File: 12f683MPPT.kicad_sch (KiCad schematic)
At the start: 47 parts, among them J1 Conn_01x01_Male, J2 Conn_01x01_Male, J3 Conn_01x01_Male, J4 Conn_01x01_Male, Q1 BUK9511-55A127, Q2 BUK9511-55A127, Q3 2N2222A, Q4 2N2222A, Q5 2N2907A, SW1 SW_Push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

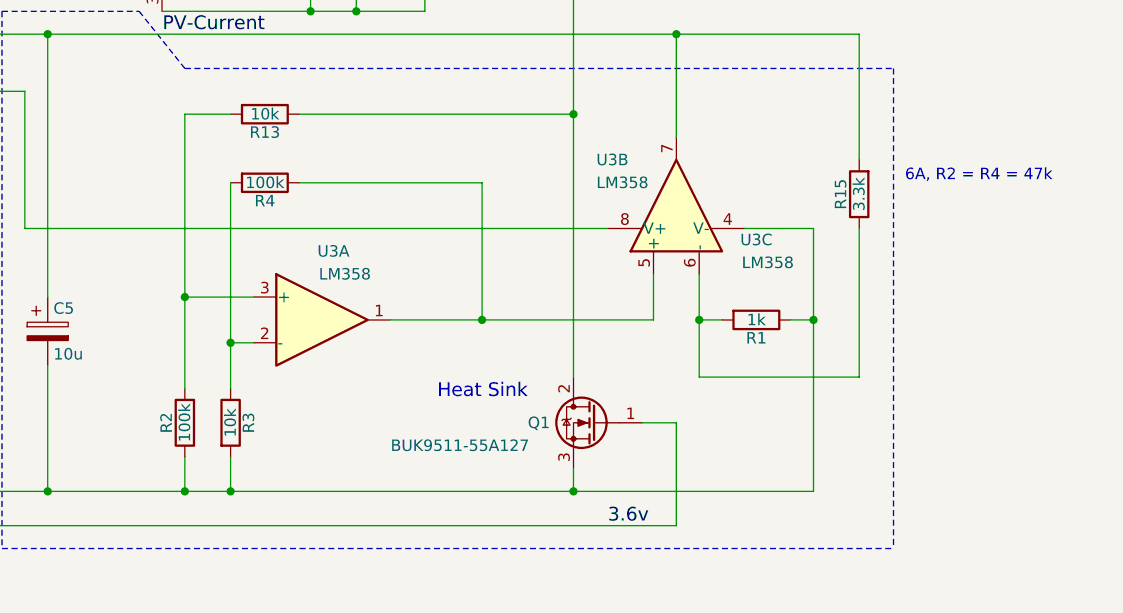
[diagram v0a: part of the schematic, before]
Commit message: Add current measurement hint.
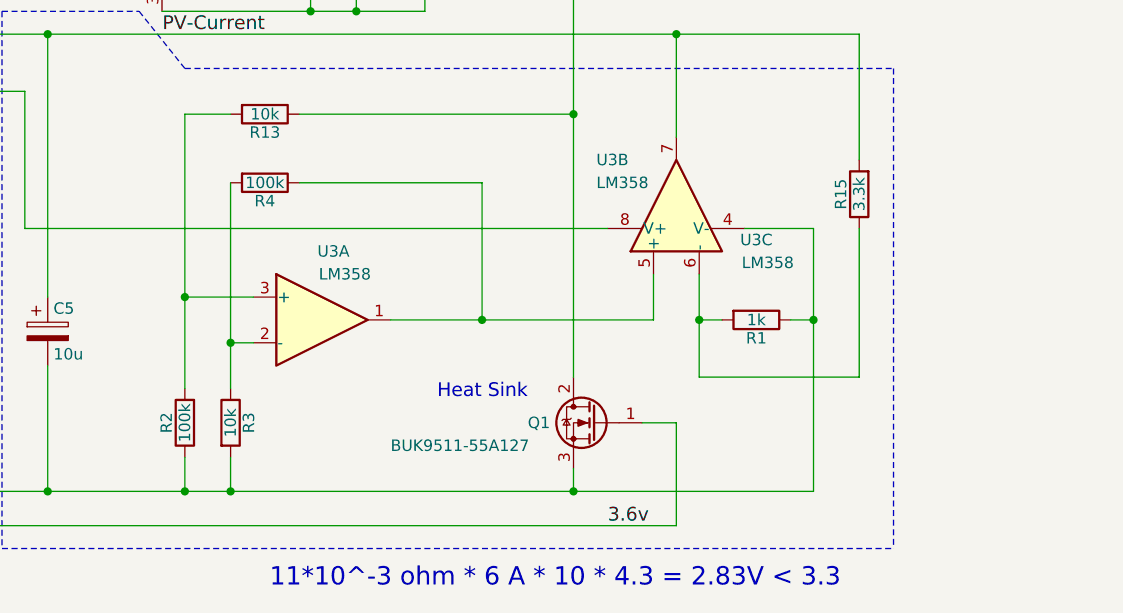
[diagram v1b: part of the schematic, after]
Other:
- note added: "11*10^-3 ohm * 6 A * 10 * 4.3 = 2.83V < 3.3"
- note removed: "6A, R2 = R4 = 47k"
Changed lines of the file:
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@@
 		)
 	)
-	(text "6A, R2 = R4 = 47k"
+	(text "11*10^-3 ohm * 6 A * 10 * 4.3 = 2.83V < 3.3"
 		(exclude_from_sim no)
-		(at 250.19 107.95 0)
+		(at 211.328 151.892 0)
 		(effects
 			(font
-				(size 1.27 1.27)
+				(size 2.032 2.032)
 			)
-			(justify left bottom)
 		)
 	)

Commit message: Update circuit.
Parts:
- added J5: Vin, Connector_Pin:Pin_D1.0mm_L10.0mm, symbol Connector:Conn_01x01_Pin
- added J6: GND, Connector_Pin:Pin_D1.0mm_L10.0mm, symbol Connector:Conn_01x01_Pin
- added J7: 12V, Connector_Pin:Pin_D1.0mm_L10.0mm, symbol Connector:Conn_01x01_Pin
- C1, C7: footprint Capacitors_THT:CP_Radial_D12.5mm_P5.00mm -> Capacitor_THT:CP_Radial_D12.5mm_P5.00mm
- C2, C3, C5: footprint Capacitors_THT:CP_Radial_D12.5mm_P5.00mm -> Capacitor_THT:CP_Radial_D8.0mm_P2.50mm
- C4: footprint Capacitors_THT:C_Disc_D7.5mm_W4.4mm_P5.00mm -> Capacitor_THT:C_Disc_D7.5mm_W4.4mm_P5.00mm
- D1, D2, D6: footprint Diodes_THT:D_DO-201AD_P15.24mm_Horizontal -> Diode_THT:D_DO-201AD_P15.24mm_Horizontal
- D4, D7, D8: footprint LEDs:LED_D3.0mm -> LED_THT:LED_D3.0mm
- D5: footprint Diodes_THT:D_DO-41_SOD81_P10.16mm_Horizontal -> Diode_THT:D_DO-41_SOD81_P10.16mm_Horizontal
- D9: footprint Diode_THT:D_DO-41_SOD81_P10.16mm_Horizontal -> Diode_THT:D_DO-41_SOD81_P5.08mm_Vertical_AnodeUp
- L1: footprint Inductors_THT:L_Toroid_Vertical_L16.0mm_W8.0mm_P7.62mm -> Inductor_THT:L_Toroid_Vertical_L16.0mm_W8.0mm_P7.62mm
- Q3, Q4, Q5: footprint TO_SOT_Packages_THT:TO-92_Inline_Wide -> Package_TO_SOT_THT:TO-92_Inline_Wide
- R1, R10, R11, R12, R13, R14, R15, R16, R2, R3, R4, R5, R6, R7, R8, R9: footprint Resistors_THT:R_Axial_DIN0309_L9.0mm_D3.2mm_P12.70mm_Horizontal -> Resistor_THT:R_Axial_DIN0309_L9.0mm_D3.2mm_P12.70mm_Horizontal
- U1: footprint TO_SOT_Packages_THT:TO-220-3_Vertical -> Package_TO_SOT_THT:TO-220-3_Vertical
- U2, U3: footprint Housings_DIP:DIP-8_W7.62mm_LongPads -> Package_DIP:DIP-8_W7.62mm_LongPads
- U3: footprint (none) -> Package_DIP:DIP-8_W7.62mm_LongPads
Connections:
- net +24V: now also J5.1 (Pin_1)
- net GNDPWR: now also J6.1 (Pin_1)
- net at D5.1 (K), U1.1 (VI): now also J7.1 (Pin_1)
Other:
- note added: "Optional"
- moved on the sheet: D5

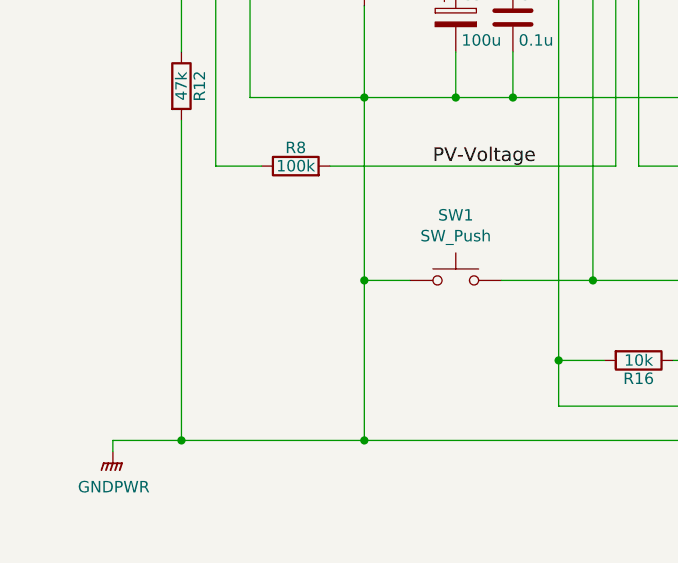
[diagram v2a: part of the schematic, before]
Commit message: Add zener for input voltage limiting.
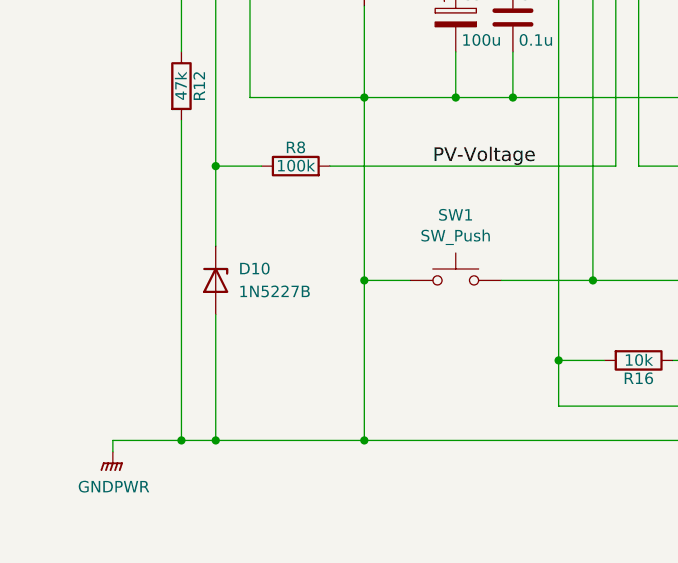
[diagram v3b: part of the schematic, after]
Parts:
- added D10: 1N5227B, Diode_THT:D_DO-41_SOD81_P7.62mm_Horizontal, symbol Device:D_Zener
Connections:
- net GNDPWR: now also D10.2 (A)
- net at R12.1, R5.2, R8.1: now also D10.1 (K)
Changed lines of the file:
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@@
 	)
 	(junction
+		(at 50.8 111.76)
+		(diameter 0)
+		(color 0 0 0 0)
+	)
+	(junction
 		(at 66.04 78.74)
 		(diameter 0)
@@
 	)
 	(junction
+		(at 50.8 142.24)
+		(diameter 0)
+		(color 0 0 0 0)
+	)
+	(junction
 		(at 67.31 124.46)
 		(diameter 0)
@@
 	(wire
 		(pts
+			(xy 50.8 111.76) (xy 50.8 120.65)
+		)
+		(stroke
+			(width 0)
+			(type default)
+		)
+	)
+	(wire
+		(pts
 			(xy 54.61 104.14) (xy 54.61 78.74)
 		)
@@
 	(wire
 		(pts
+			(xy 50.8 142.24) (xy 46.99 142.24)
+		)
+		(stroke
+			(width 0)
+			(type default)
+		)
+	)
+	(wire
+		(pts
 			(xy 83.82 78.74) (xy 83.82 73.66)
 		)
@@
 	(wire
 		(pts
-			(xy 67.31 142.24) (xy 46.99 142.24)
+			(xy 67.31 142.24) (xy 50.8 142.24)
 		)
 		(stroke
@@
 	(wire
 		(pts
+			(xy 50.8 128.27) (xy 50.8 142.24)
+		)
+		(stroke
+			(width 0)
+			(type default)
+		)
+	)
+	(wire
+		(pts
 			(xy 73.66 68.58) (xy 73.66 76.2)
 		)
@@
 					(unit 1)
 				)
+			)
+		)
+	)
+	(symbol
+		(lib_id "Device:D_Zener")
+		(at 50.8 124.46 270)
+		(unit 1)
+		(exclude_from_sim no)
+		(in_bom yes)
+		(on_board yes)
+		(dnp no)
+		(fields_autoplaced yes)
+		(property "Reference" "D10"
+			(at 53.34 123.1899 90)
+			(effects
+				(font
+					(size 1.27 1.27)
+				)
+				(justify left)
+			)
+		)
+		(property "Value" "1N5227B"
+			(at 53.34 125.7299 90)
+			(effects
+				(font
+					(size 1.27 1.27)
+				)
+				(justify left)
+			)
+		)
+		(property "Footprint" "Diode_THT:D_DO-41_SOD81_P7.62mm_Horizontal"
+			(at 50.8 124.46 0)
+			(effects
+				(font
+					(size 1.27 1.27)
+				)
+				(hide yes)
+			)
+		)
+		(property "Datasheet" "~"
+			(at 50.8 124.46 0)
+			(effects
+				(font
+					(size 1.27 1.27)
+				)
+				(hide yes)
+			)
+		)
+		(property "Description" "Zener diode"
+			(at 50.8 124.46 0)
+			(effects
+				(font
+					(size 1.27 1.27)
+				)
+				(hide yes)
+			)
+		)
+		(pin "2"
+		)
+		(pin "1"
+		)
+		(instances
+			(project ""
+				(path "/c54864ce-ba59-4422-a8c7-824cf583dfc9"
+					(reference "D10")
+					(unit 1)
+				)

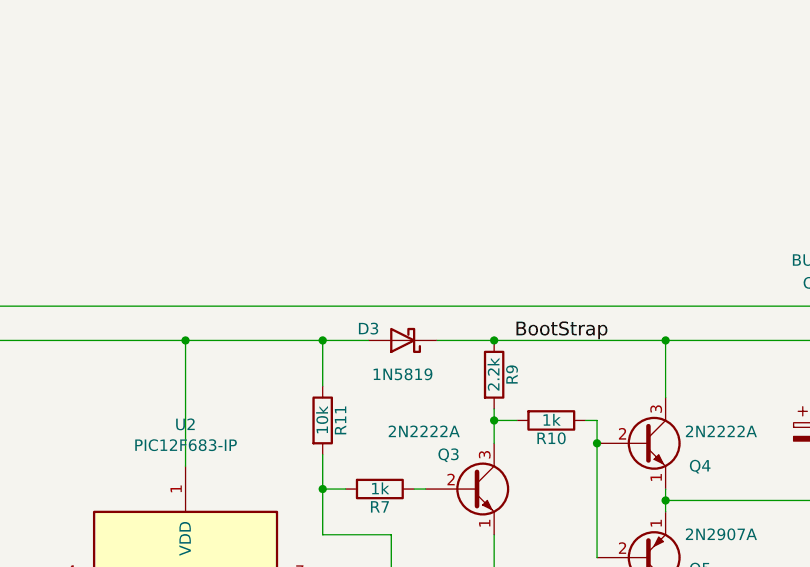
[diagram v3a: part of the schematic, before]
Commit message: Add hint for D3 alternative.
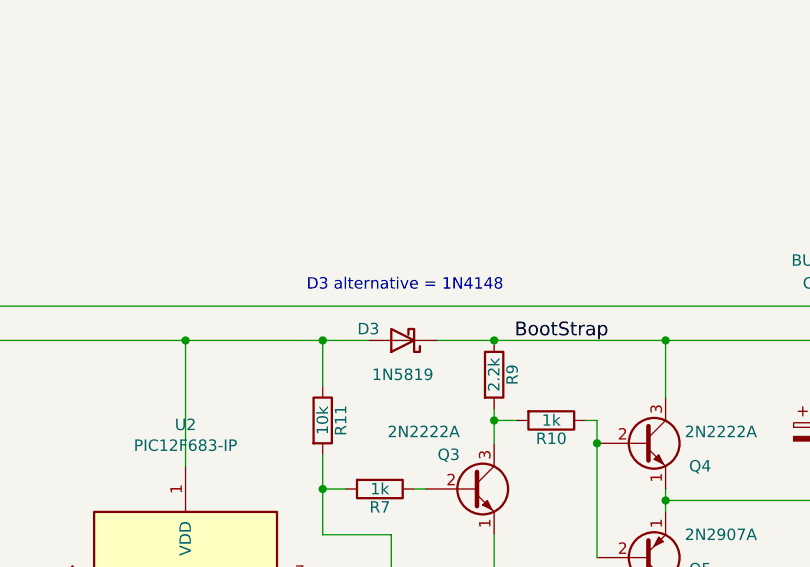
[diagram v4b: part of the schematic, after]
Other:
- note added: "D3 alternative = 1N4148"
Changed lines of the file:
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@@
+		)
+	)
+	(text "D3 alternative = 1N4148"
+		(exclude_from_sim no)
+		(at 138.684 53.594 0)
+		(effects
+			(font
+				(size 1.27 1.27)
+			)
 		)
 	)
